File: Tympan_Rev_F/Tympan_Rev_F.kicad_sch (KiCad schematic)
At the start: 89 parts, among them J1 SJ-3523-SMT-TR, J2 SJ-3524-SMT-TR-PI, J3 Conn_01x06, J4 Qwiik Connector, J7 J-Link, P1 CONN_01X06, P2 CONN_01X06, P3 CONN_01X06, P4 CONN_01X06, P6 CONN_01X01, P7 CONN_01X01, P8 CONN_01X01, SW1 CL-SB-22A, SW2 SW_Push, U1 MCP73831, U2 TLV320AIC3206IRSBT, U3 74LVC1G66, U4 LP5907MFX-1.8, U5 Teensy4.1, U6 LC709203, U7 MDBT50Q-1MV2, Y1 32.768

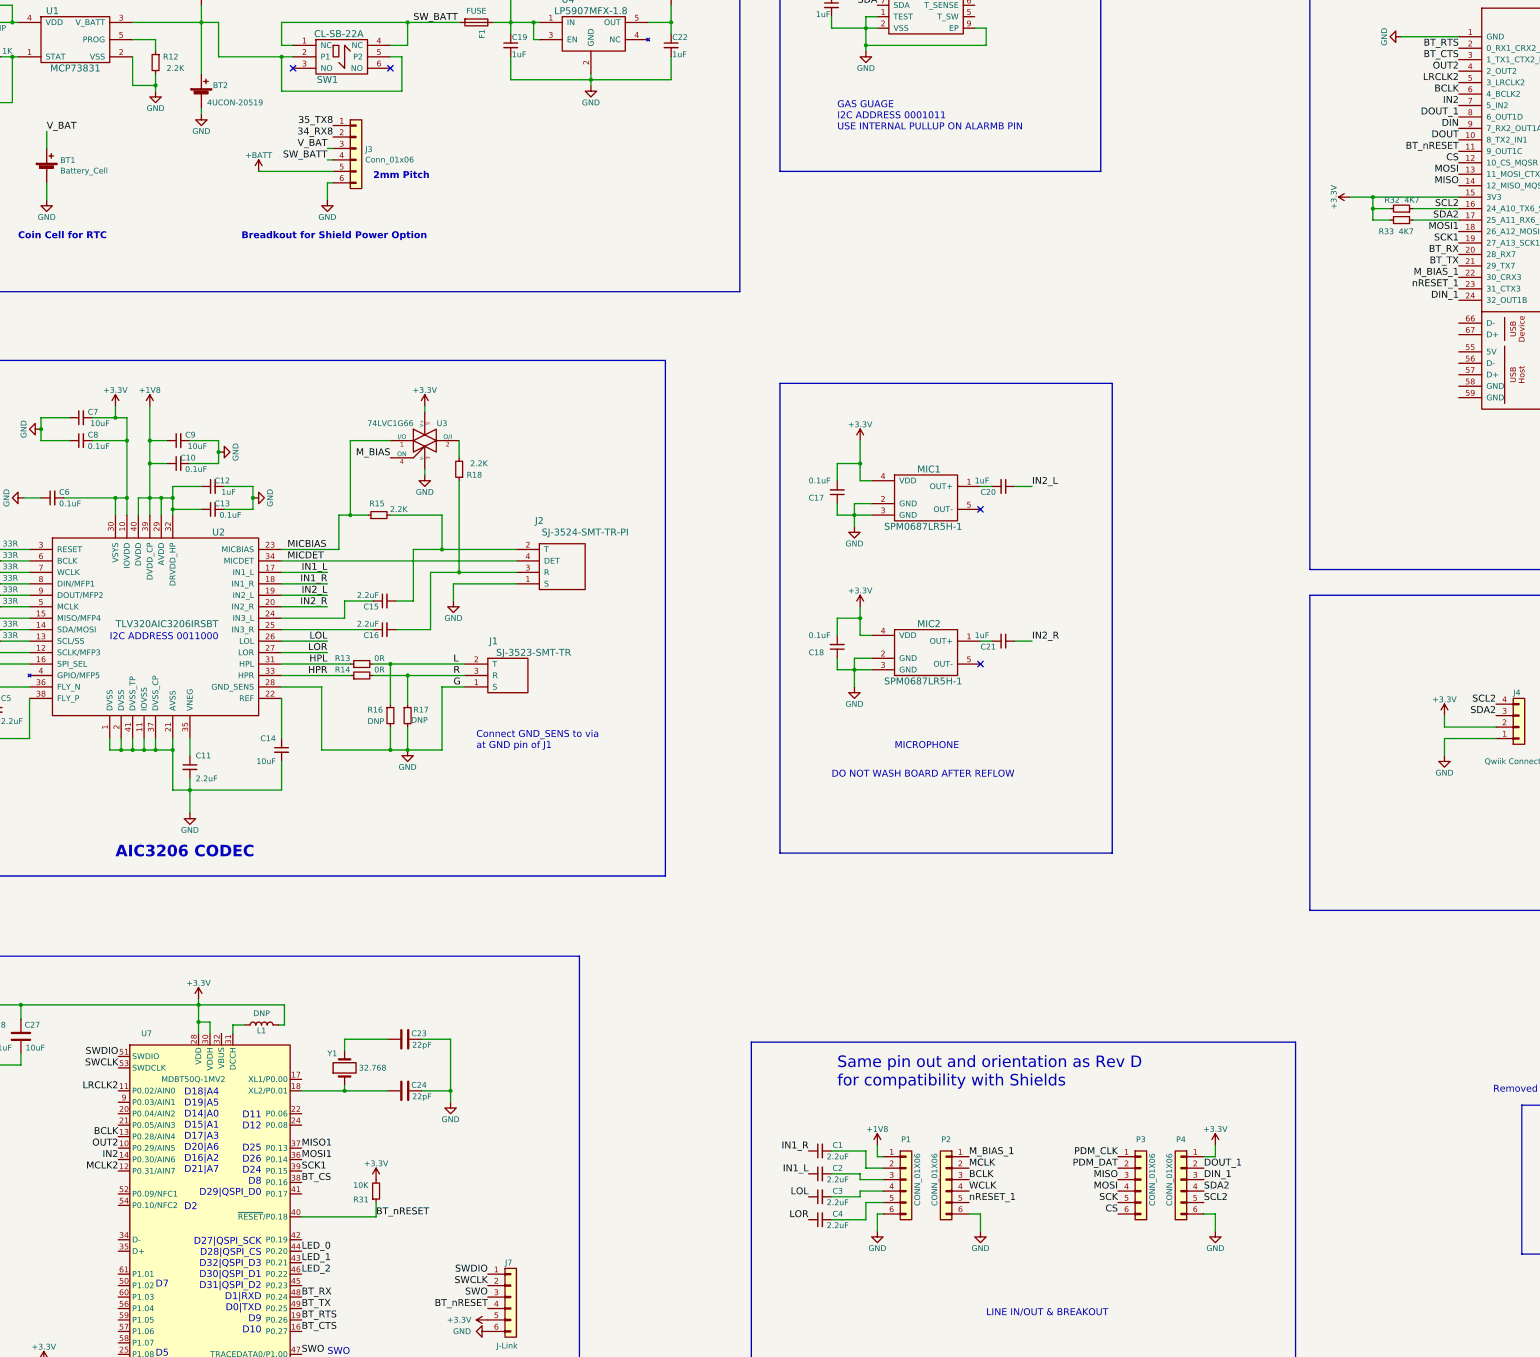
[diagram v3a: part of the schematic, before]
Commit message: First pass at routing
Have all circuits routed exept for nRF52 program header. Got to figure out the footprint and placement.
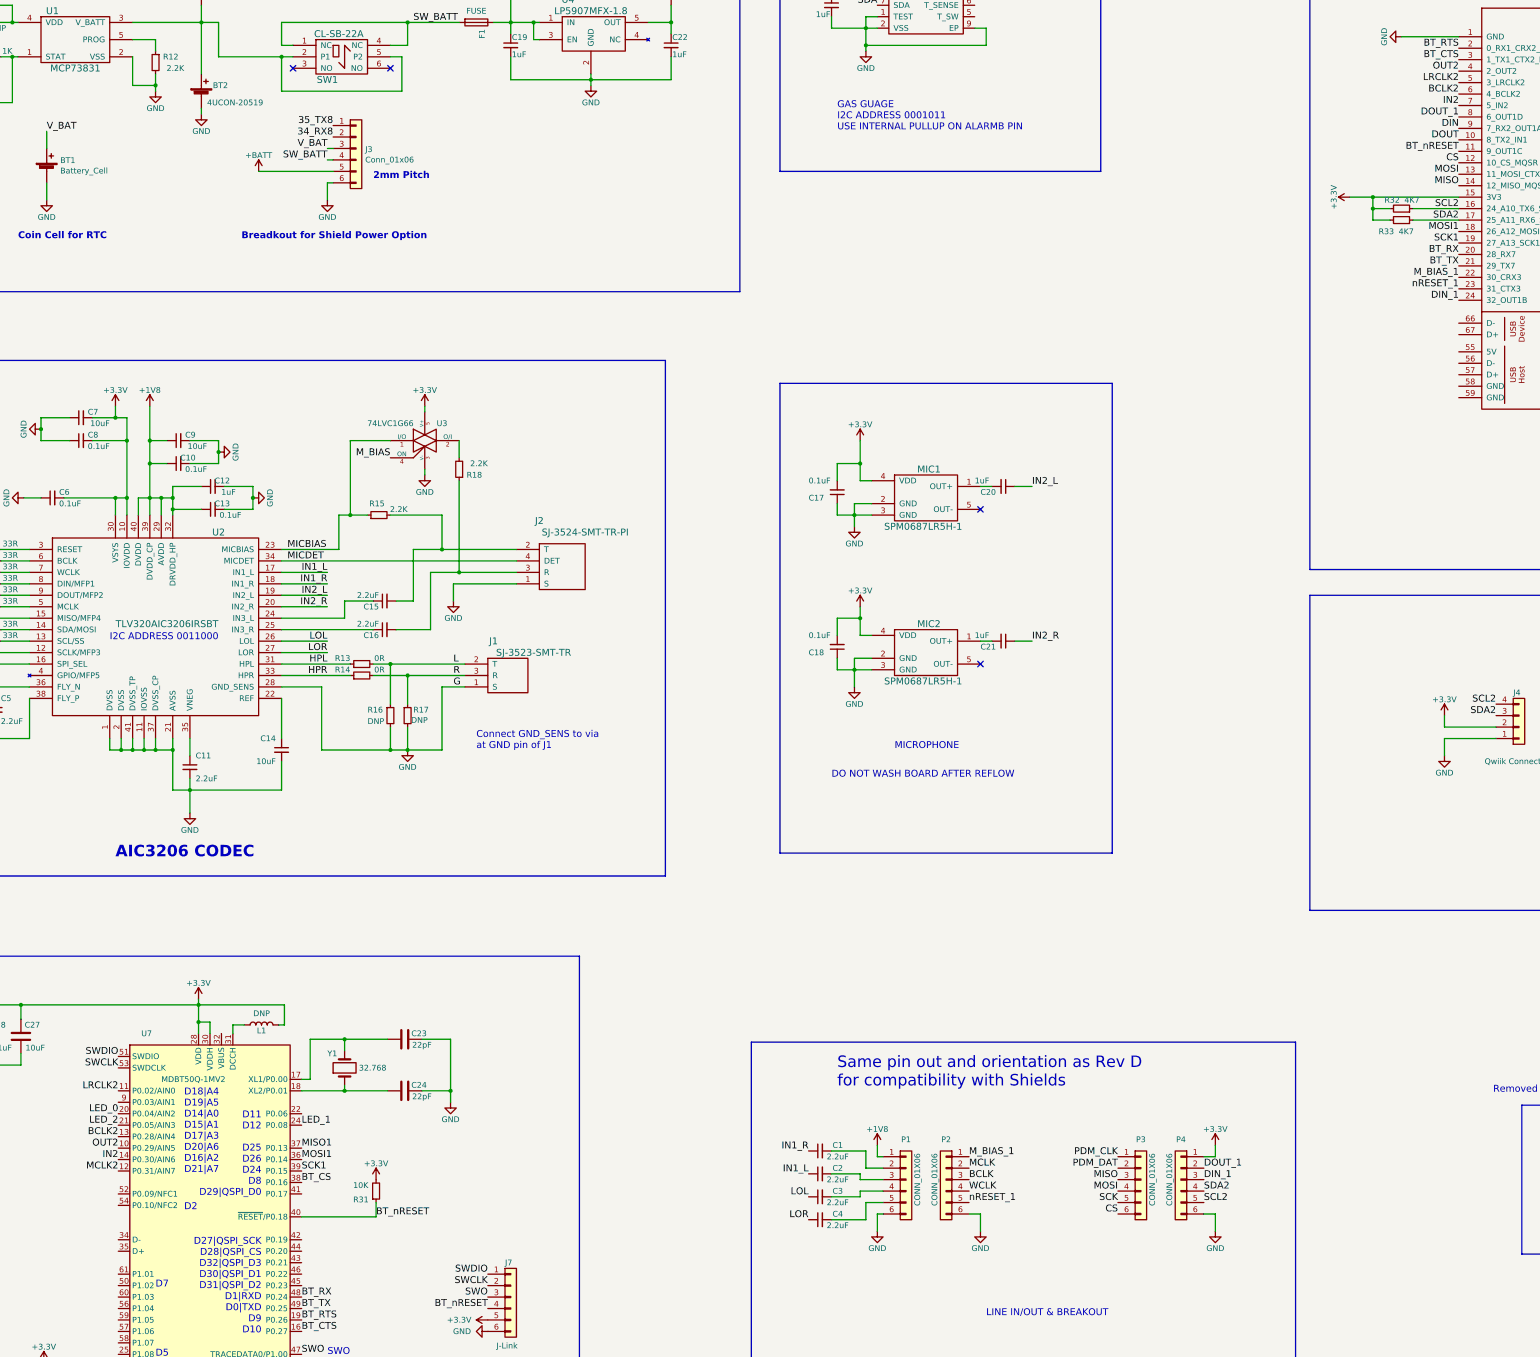
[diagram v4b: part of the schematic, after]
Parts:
- C23, C24, C27, C28: footprint (none) -> Capacitor_SMD:C_0402_1005Metric
- J7: footprint (none) -> Connector_PinHeader_2.54mm:PinHeader_2x03_P2.54mm_Vertical_SMD
- L1: footprint (none) -> Capacitor_SMD:C_0603_1608Metric
- Y1: footprint (none) -> Tympan:XTAL
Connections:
- net BCLK: no longer U5.6 (4_BCLK2), U7.13 (P0.28/AIN4)
- net LED_0: now also U7.20 (P0.04/AIN2); no longer U7.44 (P0.20)
- net LED_1: now also U7.24 (P0.08); no longer U7.43 (P0.21)
- net LED_2: now also U7.21 (P0.05/AIN3); no longer U7.46 (P0.22)
- net at U7.17 (XL1/P0.00): now also C23.1, Y1.2
- new net BCLK2: U5.6 (4_BCLK2), U7.13 (P0.28/AIN4)
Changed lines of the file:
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@@
   (junction (at 109.22 162.56) (diameter 0) (color 0 0 0 0)
   )
+  (junction (at 147.32 280.035) (diameter 0) (color 0 0 0 0)
+  )
   (junction (at 99.06 160.02) (diameter 0) (color 0 0 0 0)
   )
@@
     (stroke (width 0) (type default))
   )
+  (wire (pts (xy 139.7 280.035) (xy 147.32 280.035))
+    (stroke (width 0) (type default))
+  )
   (wire (pts (xy 57.15 72.39) (xy 73.66 72.39))
     (stroke (width 0) (type default))
@@
     (stroke (width 0) (type default))
   )
+  (wire (pts (xy 139.7 288.925) (xy 139.7 280.035))
+    (stroke (width 0) (type default))
+  )
   (wire (pts (xy 172.72 156.21) (xy 172.72 176.53))
     (stroke (width 0) (type default))
@@
     (stroke (width 0) (type default))
   )
+  (wire (pts (xy 137.795 288.925) (xy 139.7 288.925))
+    (stroke (width 0) (type default))
+  )
   (wire (pts (xy 148.59 163.83) (xy 152.4 163.83))
     (stroke (width 0) (type default))
@@
     (effects (font (size 1.524 1.524)) (justify right bottom))
   )
-  (label "LED_0" (at 137.795 327.025 0) (fields_autoplaced)
-    (effects (font (size 1.524 1.524)) (justify left bottom))
+  (label "LED_0" (at 97.155 296.545 180) (fields_autoplaced)
+    (effects (font (size 1.524 1.524)) (justify right bottom))
   )
   (label "SDA" (at 265.43 50.8 180) (fields_autoplaced)
@@
     (effects (font (size 1.524 1.524)) (justify right bottom))
   )
-  (label "LED_1" (at 137.795 329.565 0) (fields_autoplaced)
+  (label "LED_1" (at 137.795 299.085 0) (fields_autoplaced)
     (effects (font (size 1.524 1.524)) (justify left bottom))
   )
@@
     (effects (font (size 1.524 1.524)) (justify left bottom))
   )
-  (label "BCLK" (at 97.155 301.625 180) (fields_autoplaced)
+  (label "BCLK2" (at 97.155 301.625 180) (fields_autoplaced)
     (effects (font (size 1.524 1.524)) (justify right bottom))
   )
-  (label "LED_2" (at 137.795 332.105 0) (fields_autoplaced)
-    (effects (font (size 1.524 1.524)) (justify left bottom))
+  (label "LED_2" (at 97.155 299.085 180) (fields_autoplaced)
+    (effects (font (size 1.524 1.524)) (justify right bottom))
   )
   (label "M_BIAS_1" (at 285.75 306.07 0) (fields_autoplaced)
@@
     (effects (font (size 1.524 1.524)) (justify left bottom))
   )
-  (label "BCLK" (at 394.335 70.485 180) (fields_autoplaced)
+  (label "BCLK2" (at 394.335 70.485 180) (fields_autoplaced)
     (effects (font (size 1.524 1.524)) (justify right bottom))
   )
@@
       (effects (font (size 1.27 1.27)))
     )
-    (property "Footprint" "" (at 128.905 276.86 0)
+    (property "Footprint" "Capacitor_SMD:C_0603_1608Metric" (at 128.905 276.86 0)
       (effects (font (size 1.27 1.27)) hide)
     )
@@
       (effects (font (size 1.27 1.27)))
     )
-    (property "Footprint" "" (at 164.465 290.4998 0)
+    (property "Footprint" "Capacitor_SMD:C_0402_1005Metric" (at 164.465 290.4998 0)
       (effects (font (size 1.27 1.27)) hide)
     )
@@
       (effects (font (size 1.27 1.27)))
     )
-    (property "Footprint" "" (at 66.9798 275.59 0)
+    (property "Footprint" "Capacitor_SMD:C_0402_1005Metric" (at 66.9798 275.59 0)
       (effects (font (size 1.27 1.27)) hide)
     )
@@
       (effects (font (size 1.27 1.27)) (justify left))
     )
-    (property "Footprint" "" (at 184.15 337.185 0)
+    (property "Footprint" "Connector_PinHeader_2.54mm:PinHeader_2x03_P2.54mm_Vertical_SMD" (at 184.15 337.185 0)
       (effects (font (size 1.27 1.27)) hide)
     )
@@
       (effects (font (size 1.27 1.27)))
     )
-    (property "Footprint" "" (at 164.465 279.0698 0)
+    (property "Footprint" "Capacitor_SMD:C_0402_1005Metric" (at 164.465 279.0698 0)
       (effects (font (size 1.27 1.27)) hide)
     )
@@
       (effects (font (size 1.27 1.27)) (justify right))
     )
-    (property "Footprint" "" (at 147.32 286.385 0)
+    (property "Footprint" "Tympan:XTAL" (at 147.32 286.385 0)
       (effects (font (size 1.27 1.27)) hide)
     )
@@
       (effects (font (size 1.27 1.27)))
     )
-    (property "Footprint" "" (at 74.5998 275.59 0)
+    (property "Footprint" "Capacitor_SMD:C_0402_1005Metric" (at 74.5998 275.59 0)
       (effects (font (size 1.27 1.27)) hide)
     )
